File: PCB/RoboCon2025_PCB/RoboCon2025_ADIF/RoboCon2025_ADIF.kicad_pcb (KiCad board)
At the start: 2 copper layers, 60 x 52 mm, 35 parts, among them J1 Conn_01x05, J2 1x9, J3 Conn_01x09, J4 S2B-XH-A, J5 Micro_SD_Card_Det_Hirose_DM3AT, J6 S3B-XH-A, J7 S2B-XH-A, J8 S2B-XH-A, J9 S3B-XH-A, U1 PCM5102A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

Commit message: ADIF 編集
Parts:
- moved J5 35.7 mm to (160.2, 71.9), turned to 180 degrees
- moved J9 35.5 mm to (166.5, 107.5), turned to 90 degrees
- moved J4 33.2 mm to (158.0, 105.0), turned to 0 degrees
- moved C1 27.4 mm to (164.6, 82.0), turned to 0 degrees
- moved R6 25.3 mm to (143.0, 105.1)
- moved C8 25.1 mm to (143.0, 99.1)
- moved R5 20.2 mm to (150.1, 80.0), turned to 180 degrees
- moved U2 19.1 mm to (149.5, 101.5), turned to 90 degrees
- moved JP1 19.0 mm to (128.7, 77.0)
- moved R3 18.3 mm to (156.4, 84.2), turned to 180 degrees
- moved D2 17.6 mm to (164.0, 97.0), turned to 0 degrees
- moved R2 15.6 mm to (156.4, 87.7), turned to 180 degrees
- moved J2 15.2 mm to (132.1, 109.2)
- moved J3 15.2 mm to (132.1, 94.0)
- moved R1 14.1 mm to (156.4, 91.2), turned to 180 degrees
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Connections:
- J6 pad 1: /AUDIO_OUT_L -> GNDA
- J6 pad 2: /AUDIO_OUT_R -> /AUDIO_OUT_L
- J6 pad 3: GNDA -> /AUDIO_OUT_R
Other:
- board text added: "ADIF(Tx)"

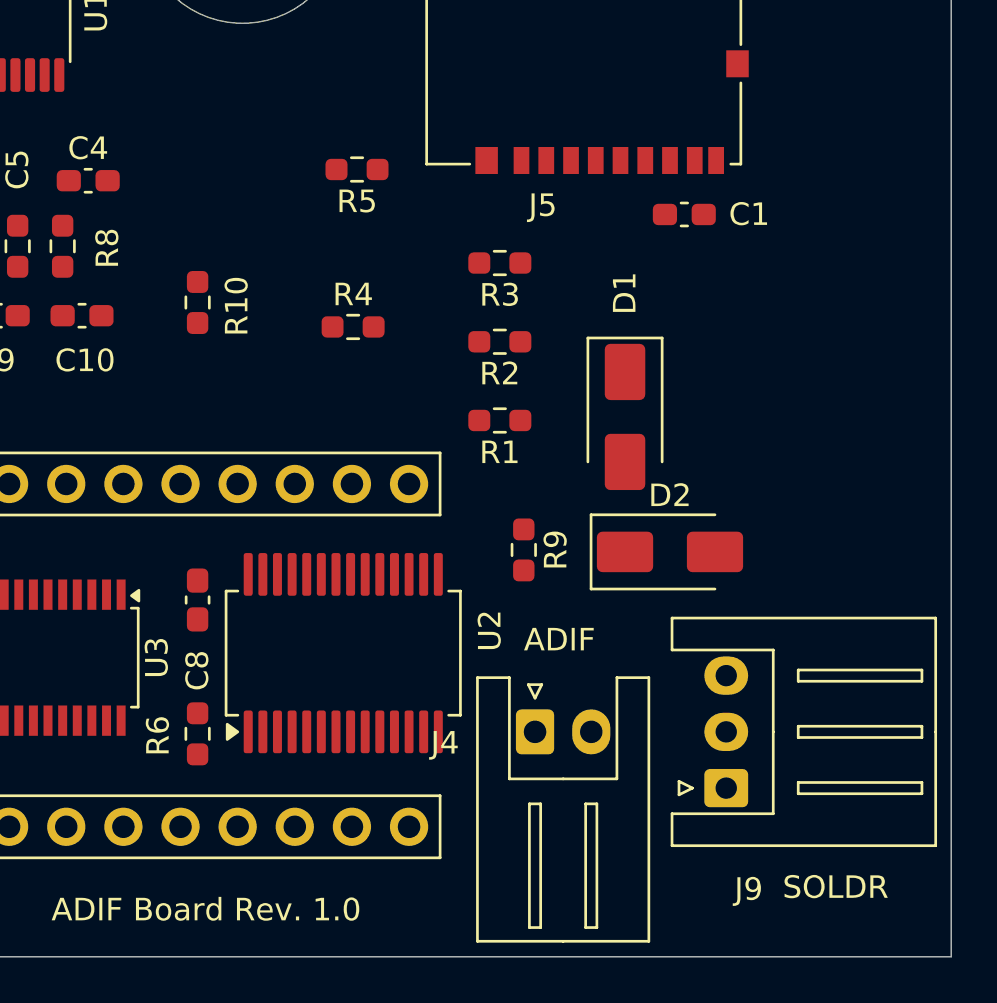
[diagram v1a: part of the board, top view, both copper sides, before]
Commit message: [PCB] ADIF基板のIOエキスパンダ部品変更
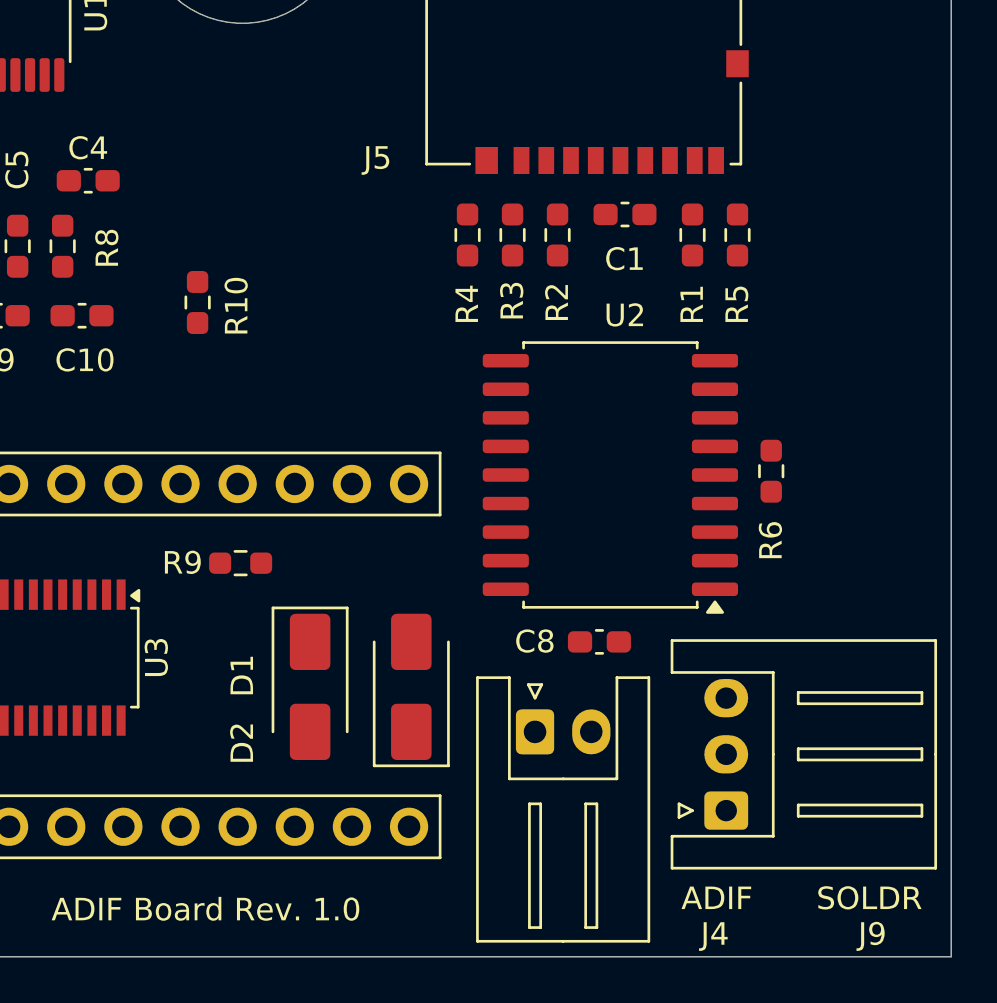
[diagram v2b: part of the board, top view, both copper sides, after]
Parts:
- U2: value MCP23017_SS -> MCP23008-xSO; footprint Package_SO:SSOP-28_5.3x10.2mm_P0.65mm -> Package_SO:SOIC-18W_7.5x11.6mm_P1.27mm
- moved R6 28.0 mm to (168.5, 93.4)
- moved C8 18.0 mm to (160.9, 101.0), turned to 180 degrees
- moved R5 17.2 mm to (167.0, 82.9), turned to 90 degrees
- moved D2 17.1 mm to (148.0, 103.0), turned to -90 degrees
- moved D1 15.3 mm to (152.5, 103.0), turned to 90 degrees
- moved U2 14.3 mm to (161.3, 93.6), turned to 180 degrees
- moved R9 12.6 mm to (144.9, 97.5), turned to 0 degrees
- moved R1 11.9 mm to (165.0, 82.9), turned to 90 degrees
- moved R4 6.53 mm to (155.0, 82.9), turned to 90 degrees
- moved R2 5.39 mm to (159.0, 82.9), turned to 90 degrees
- moved C1 2.64 mm to (162.0, 82.0)
- moved R3 1.37 mm to (157.0, 82.9), turned to 90 degrees
- moved J9 1.00 mm to (166.5, 108.5)
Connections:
- R6 pad 1: +3V3 -> Net-(U2-~{RESET})
- R6 pad 2: Net-(U2-~{RESET}) -> +3V3
- U2 pad 1: ACT_N -> /EXT_3SCL
- U2 pad 10: GND -> ACT_N
- U2 pad 11: unconnected-(U2-NC-Pad11) -> MUTE_N
- U2 pad 12: /EXT_3SDA -> Net-(U2-GP2)
- U2 pad 13: /EXT_3SCL -> Net-(U2-GP3)
- U2 pad 14: unconnected-(U2-NC-Pad14) -> Net-(U2-GP4)
- U2 pad 15: GND -> Net-(U2-GP5)
- U2 pad 16: GND -> unconnected-(U2-GP6-Pad16)
- U2 pad 17: GND -> unconnected-(U2-GP7-Pad17)
- U2 pad 18: Net-(U2-~{RESET}) -> +3V3
- U2 pad 2: unconnected-(U2-GPB1-Pad2) -> /EXT_3SDA
- U2 pad 3: unconnected-(U2-GPB2-Pad3) -> GND
- U2 pad 4: unconnected-(U2-GPB3-Pad4) -> GND
- U2 pad 5: unconnected-(U2-GPB4-Pad5) -> GND
- U2 pad 6: unconnected-(U2-GPB5-Pad6) -> Net-(U2-~{RESET})
- U2 pad 9: +3V3 -> GND
- U3 pad 1: Net-(U2-GPA1) -> Net-(U2-GP2)
- U3 pad 2: Net-(U2-GPA2) -> Net-(U2-GP3)
- U3 pad 3: Net-(U2-GPA3) -> Net-(U2-GP4)
- U3 pad 4: Net-(U2-GPA4) -> Net-(U2-GP5)

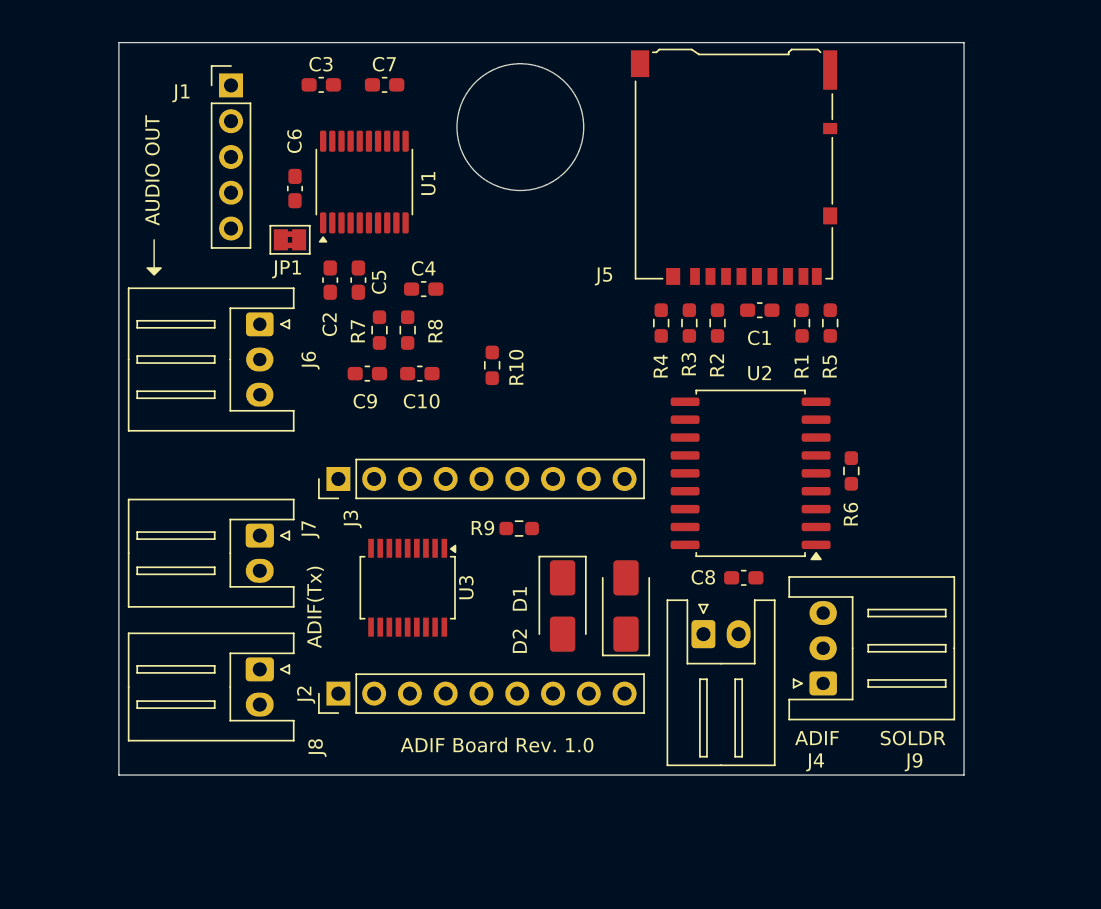
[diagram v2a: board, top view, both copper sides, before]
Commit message: [PCB] update: BB基板のパターン引いた(未配線あり)
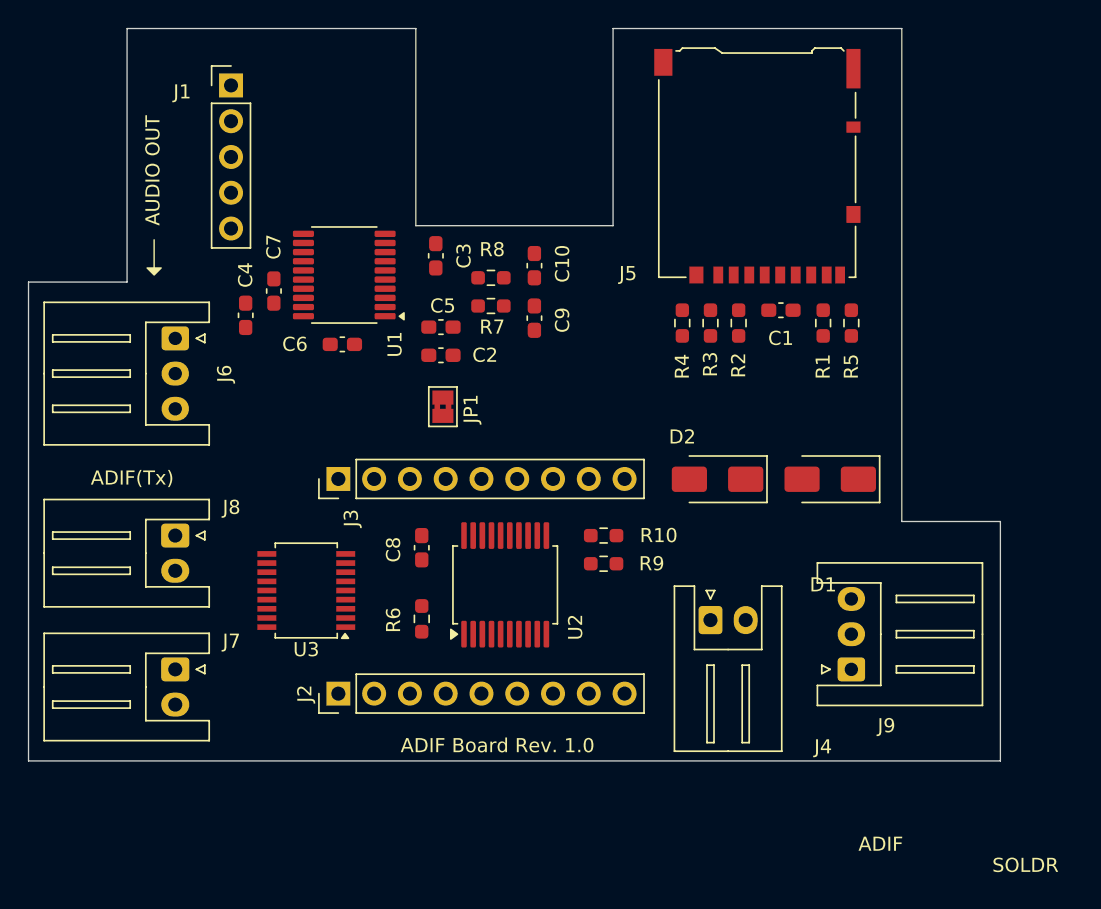
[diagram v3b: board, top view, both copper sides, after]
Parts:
- U2: value MCP23008-xSO -> MCP23008-xSS; footprint Package_SO:SOIC-18W_7.5x11.6mm_P1.27mm -> Package_SO:SSOP-20_5.3x7.2mm_P0.65mm
- moved R6 32.3 mm to (138.0, 103.9), turned to 90 degrees
- moved C8 23.0 mm to (138.0, 98.9), turned to 90 degrees
- moved U2 19.1 mm to (143.9, 101.5), turned to 90 degrees
- moved D1 17.1 mm to (167.0, 94.0), turned to 180 degrees
- moved C7 16.6 mm to (127.5, 80.6), turned to -90 degrees
- moved JP1 16.1 mm to (139.5, 88.8), turned to 90 degrees
- moved C3 14.6 mm to (139.0, 78.1), turned to 90 degrees
- moved R10 14.4 mm to (150.9, 98.0), turned to 180 degrees
- moved D2 14.2 mm to (159.0, 94.0), turned to 180 degrees
- moved C4 12.8 mm to (125.5, 82.4), turned to 90 degrees
- moved C9 12.5 mm to (146.0, 82.6), turned to -90 degrees
- moved C6 11.6 mm to (132.4, 84.4), turned to 0 degrees
- moved J7 11.2 mm to (120.5, 107.5)
- moved J8 11.2 mm to (120.5, 98.0)
- moved C10 11.2 mm to (146.0, 78.8), turned to 90 degrees
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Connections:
- C7 pad 2: GNDA -> GND
- U1 pad 10: GNDA -> GND
- U1 pad 11: GNDA -> GND
- U1 pad 12: GNDA -> GND
- U1 pad 16: GNDA -> GND
- U1 pad 19: GNDA -> GND
- U2 pad 10: ACT_N -> unconnected-(U2-NC-Pad10)
- U2 pad 11: MUTE_N -> unconnected-(U2-NC-Pad11)
- U2 pad 12: Net-(U2-GP2) -> ACT_N
- U2 pad 13: Net-(U2-GP3) -> MUTE_N
- U2 pad 16: unconnected-(U2-GP6-Pad16) -> Net-(U2-GP4)_1
- U2 pad 17: unconnected-(U2-GP7-Pad17) -> Net-(U2-GP5)_1
- U2 pad 18: +3V3 -> unconnected-(U2-GP6-Pad18)
- U3 pad 1: Net-(U2-GP2) -> Net-(U2-GP4)
- U3 pad 2: Net-(U2-GP3) -> Net-(U2-GP5)
- U3 pad 3: Net-(U2-GP4) -> Net-(U2-GP4)_1
- U3 pad 4: Net-(U2-GP5) -> Net-(U2-GP5)_1
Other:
- board size 60 x 52 mm -> 69 x 52 mm
